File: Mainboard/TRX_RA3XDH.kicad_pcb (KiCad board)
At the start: 2 copper layers, 100 x 100 mm, 203 parts, among them J1 RF_INOUT, J10 MIC_GAIN, J12 PWR, J13 S-Met., J2 VFO, J3 PWR, J4 MIC, J5 VOL, J6 SPK, J8 PTT, J9 CW_KEY, K2 G5V-2, Q1 2N4416, Q10 2N3904, Q12 2N3904, Q2 2N918, Q3 2N4416, Q4 2N918, Q5 2N3904, Q6 2N3904, Q7 2N3904, Q8 2N3904, Q9 2N3906, U1 NE5534, U2 LM386, U3 NE5534, Y1 8.867Mhz, Y2 8.867Mhz, Y3 8.867Mhz, Y4 8.867Mhz, Y5 8.867Mhz, Y6 8.867Mhz, Y7 8.867Mhz, Y8 8.867Mhz

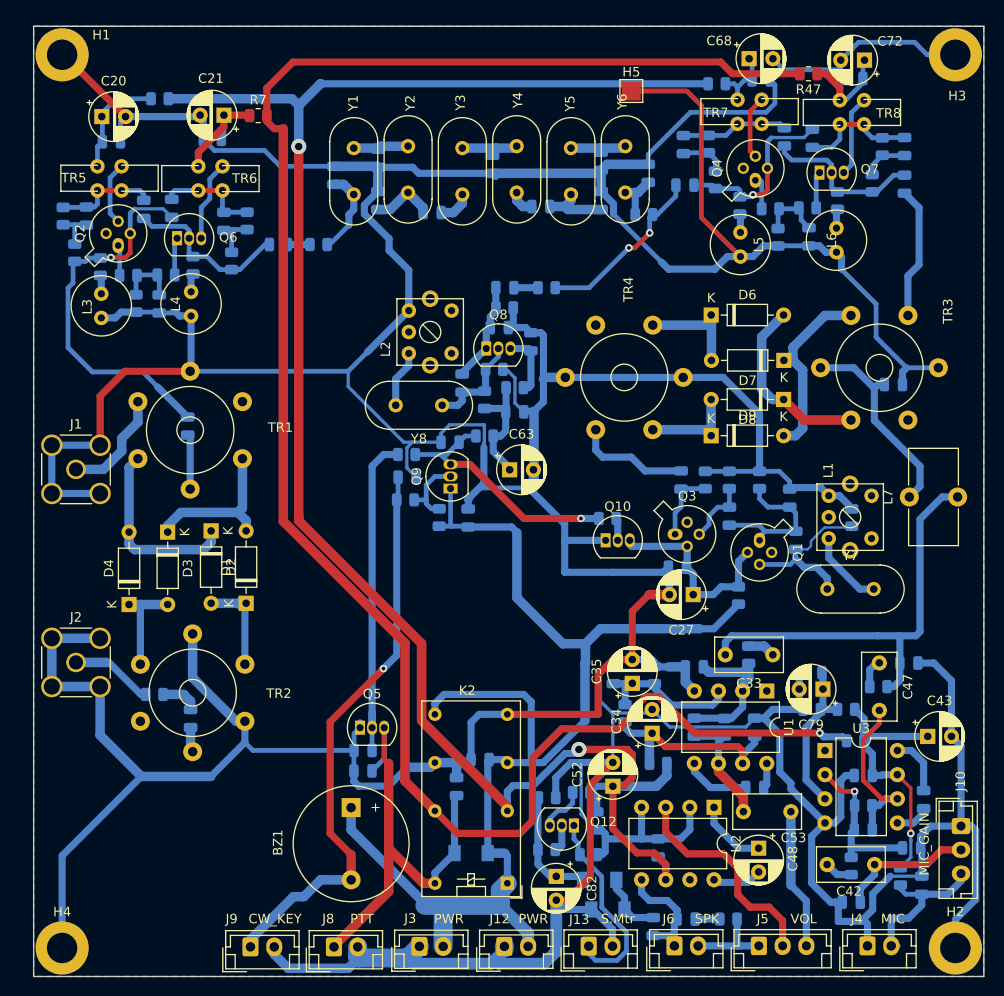
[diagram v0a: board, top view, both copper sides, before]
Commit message: Mainboard is opearational, assembled and tested
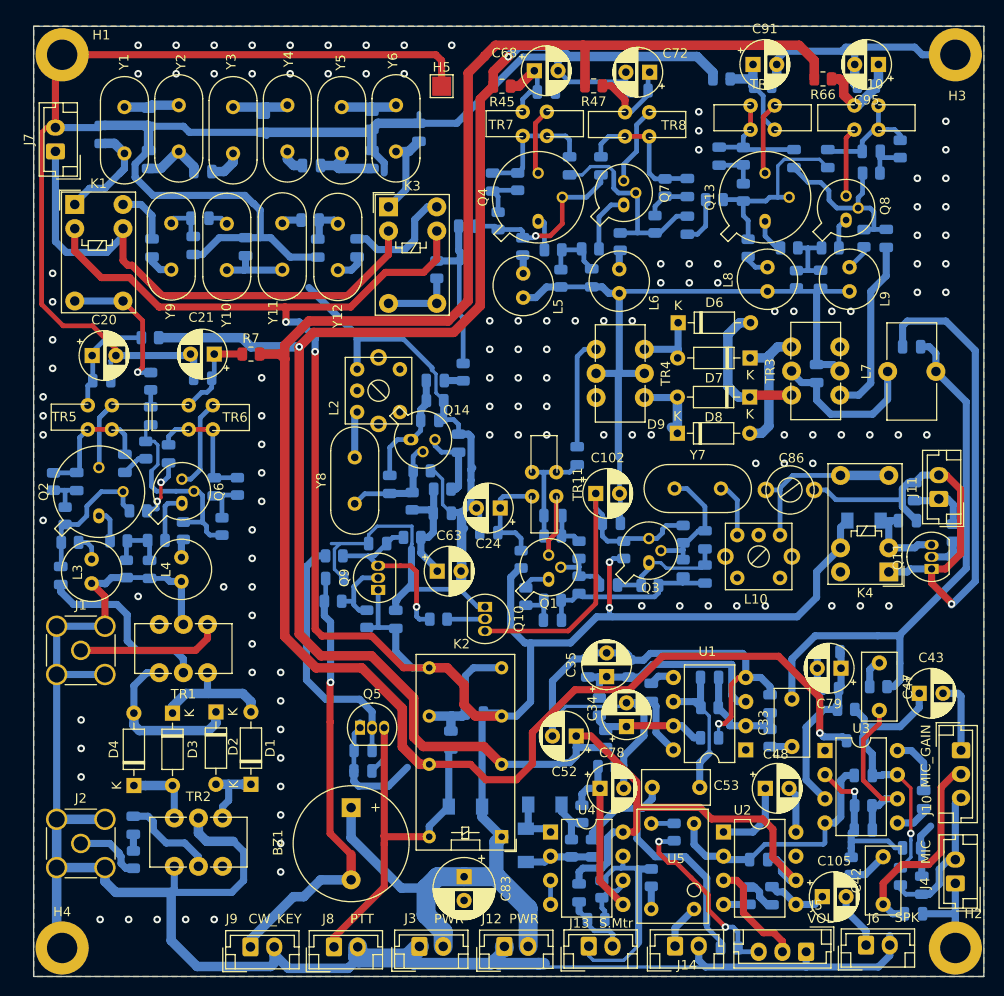
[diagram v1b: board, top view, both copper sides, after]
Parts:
- removed D13, D14: LL4148, Diode_SMD:D_MiniMELF
- removed L1: 3u, NEOSID:NEOSID_5t_4.5x4.5mm_132
- removed Q12: 2N3904, Package_TO_SOT_THT:TO-92_Inline
- added C100: 470p, Capacitor_SMD:C_0805_2012Metric, B.Cu at (109.1, 65.4)
- added C101: 0.1u, Capacitor_SMD:C_0805_2012Metric, B.Cu at (140.8, 97.3)
- added C102: 10u, Capacitor_THT:CP_Radial_D5.0mm_P2.50mm, F.Cu at (139.2, 94.2)
- added C103: 0.1u, Capacitor_SMD:C_0805_2012Metric, B.Cu at (134.6, 107.5)
- added C104: 0.1u, Capacitor_SMD:C_0805_2012Metric, B.Cu at (134.7, 96.5)
- added C105: 10u, Capacitor_THT:CP_Radial_D5.0mm_P2.50mm, F.Cu at (163.0, 136.6)
- added C49: 240p, Capacitor_SMD:C_0805_2012Metric, B.Cu at (92.5, 68.3)
- added C55: 240p, Capacitor_SMD:C_0805_2012Metric, B.Cu at (96.8, 68.1)
- added C81: 390p, Capacitor_SMD:C_0805_2012Metric, B.Cu at (102.3, 68.2)
- added C84: 240p, Capacitor_SMD:C_0805_2012Metric, B.Cu at (109.9, 68.3)
- added C85: 240p, Capacitor_SMD:C_0805_2012Metric, B.Cu at (114.0, 68.3)
- added C86: CTRIM, Ctrimm:Ctrimm_5mm, F.Cu at (159.6, 93.8)
- added C87: 0.1u, Capacitor_SMD:C_0805_2012Metric, B.Cu at (172.0, 97.0)
- added C88: 0.1u, Capacitor_SMD:C_0805_2012Metric, B.Cu at (172.7, 94.0)
- added C89: 0.1u, Capacitor_SMD:C_0805_2012Metric, B.Cu at (156.7, 51.3)
- added C90: 0.1u, Capacitor_SMD:C_0805_2012Metric, B.Cu at (152.1, 58.7)
- added C91: 10u, Capacitor_THT:CP_Radial_D5.0mm_P2.50mm, F.Cu at (155.7, 49.0)
- added C92: 10n, Capacitor_SMD:C_0805_2012Metric, B.Cu at (160.0, 58.9)
- added C93: 10n, Capacitor_SMD:C_0805_2012Metric, B.Cu at (163.6, 58.9)
- added C94: 0.1u, Capacitor_SMD:C_0805_2012Metric, B.Cu at (162.8, 71.6)
- added C95: 10u, Capacitor_THT:CP_Radial_D5.0mm_P2.50mm, F.Cu at (168.9, 49.0)
- added C96: 0.1u, Capacitor_SMD:C_0805_2012Metric, B.Cu at (168.1, 58.2)
- added C97: 0.1u, Capacitor_SMD:C_0805_2012Metric, B.Cu at (167.6, 51.3)
- added C98: 0.1u, Capacitor_SMD:C_0805_2012Metric, B.Cu at (169.7, 67.3)
- added C99: 470p, Capacitor_SMD:C_0805_2012Metric, B.Cu at (97.5, 65.2)
- added D11: LL4148, Diode_SMD:D_MiniMELF, B.Cu at (131.8, 131.2)
- added D12: LL4148, Diode_SMD:D_MiniMELF, B.Cu at (133.8, 126.9)
- added D5: LL4148, Diode_SMD:D_MiniMELF, B.Cu at (167.4, 97.0)
- added J11: USB, Connector_JST:JST_EH_B2B-EH-A_1x02_P2.50mm_Vertical, F.Cu at (175.3, 94.7)
- added J14: AGC, Connector_JST:JST_EH_B2B-EH-A_1x02_P2.50mm_Vertical, F.Cu at (147.5, 141.8)
- added J7: CW_FLT, Connector_JST:JST_EH_B2B-EH-A_1x02_P2.50mm_Vertical, F.Cu at (82.3, 58.2)
- added K1: G5V-1, Relay_THT:Relay_SPDT_Omron_G5V-1, F.Cu at (84.3, 63.8)
- added K3: G5V-1, Relay_THT:Relay_SPDT_Omron_G5V-1, F.Cu at (117.3, 64.0)
- added K4: G5V-1, Relay_THT:Relay_SPDT_Omron_G5V-1, F.Cu at (170.0, 102.4)
- added L10: 3u, NEOSID:NEOSID_5t_4.5x4.5mm_132, F.Cu at (154.1, 98.5)
- added L8: 33u, Inductor:L2.5x6, F.Cu at (157.2, 71.6)
- added L9: 33u, Inductor:L2.5x6, F.Cu at (165.9, 71.6)
- added Q11: 2N3904, Package_TO_SOT_THT:TO-92_Inline, F.Cu at (174.5, 102.1)
- added Q13: 2N5109, Package_TO_SOT_THT:TO-5-3, F.Cu at (157.0, 65.5)
- added Q14: 2N2222, Package_TO_SOT_THT:TO-18-3, F.Cu at (119.7, 88.5)
- added R54: 22k, Resistor_SMD:R_0805_2012Metric, B.Cu at (176.8, 98.3)
- added R55: 47, Resistor_SMD:R_0805_2012Metric, B.Cu at (151.6, 63.2)
- added R56: 470, Resistor_SMD:R_0805_2012Metric, B.Cu at (154.7, 62.5)
- added R61: 470, Resistor_SMD:R_0805_2012Metric, B.Cu at (155.2, 68.3)
- added R62: 2.2k, Resistor_SMD:R_0805_2012Metric, B.Cu at (154.7, 58.7)
- added R63: 4.7, Resistor_SMD:R_0805_2012Metric, B.Cu at (159.5, 68.3)
- added R64: 47, Resistor_SMD:R_0805_2012Metric, B.Cu at (152.4, 50.5)
- added R65: 100, Resistor_SMD:R_0805_2012Metric, B.Cu at (160.3, 71.6)
- added R66: 47, Resistor_SMD:R_0805_2012Metric, F.Cu at (163.1, 50.5)
- added R67: 8.2, Resistor_SMD:R_0805_2012Metric, B.Cu at (163.8, 68.3)
- added R68: 2.2k, Resistor_SMD:R_0805_2012Metric, B.Cu at (171.2, 57.9)
- added R69: 270, Resistor_SMD:R_0805_2012Metric, B.Cu at (168.1, 60.5)
- added R70: 470, Resistor_SMD:R_0805_2012Metric, B.Cu at (167.4, 67.3)
- added R71: 360, Resistor_SMD:R_0805_2012Metric, B.Cu at (144.8, 103.8)
- added R72: 6.8k, Resistor_SMD:R_0805_2012Metric, B.Cu at (148.3, 102.0)
- added R73: 13k, Resistor_SMD:R_0805_2012Metric, B.Cu at (148.3, 98.5)
- added R74: 270, Resistor_SMD:R_0805_2012Metric, B.Cu at (142.1, 100.1)
- added R75: 2.2k, Resistor_SMD:R_0805_2012Metric, B.Cu at (134.6, 98.7)
- added R76: 100, Resistor_SMD:R_0805_2012Metric, B.Cu at (145.0, 134.6)
- added R77: 2k, Resistor_SMD:R_0805_2012Metric, B.Cu at (153.2, 142.0)
- added R78: 10k*, Resistor_SMD:R_0805_2012Metric, B.Cu at (139.2, 139.0)
- added R79: 10k, Resistor_SMD:R_0805_2012Metric, B.Cu at (139.8, 135.8)
- added R80: 33*, Resistor_SMD:R_0805_2012Metric, B.Cu at (91.0, 96.0)
- added R81: 33*, Resistor_SMD:R_0805_2012Metric, B.Cu at (91.8, 89.6)
- added R82: 1k, Resistor_SMD:R_0805_2012Metric, B.Cu at (147.4, 129.8)
- added TR10: FT37-43, Inductor:L_Toroid_Vertical_L10.0mm_W5.0mm_4pin, F.Cu at (167.6, 53.3)
- added TR11: FT37-43, Inductor:L_Toroid_Vertical_L10.0mm_W5.0mm_4pin, F.Cu at (135.0, 93.2)
- added TR9: FT37-43, Inductor:L_Toroid_Vertical_L10.0mm_W5.0mm_4pin, F.Cu at (156.7, 53.3)
- added U4: LM358, Package_DIP:DIP-8_W7.62mm, F.Cu at (134.4, 129.8)
- added U5: LCR0202, Vactrol:lcr0202, F.Cu at (145.0, 137.9)
- added Y10: 8Mhz, Crystal:Crystal_HC49-U_Vertical, F.Cu at (100.3, 65.8)
- added Y11: 8Mhz, Crystal:Crystal_HC49-U_Vertical, F.Cu at (106.2, 70.6)
- added Y12: 8Mhz, Crystal:Crystal_HC49-U_Vertical, F.Cu at (112.0, 65.8)
- added Y9: 8Mhz, Crystal:Crystal_HC49-U_Vertical, F.Cu at (94.5, 70.6)
- C10, C14: value 120p -> 100p
- C11, C13: value 370p -> 330p
- C12: value 130p -> 120p
- C15, C9: value 94p -> 100p
- C16, C8: value 43p -> 39p
- C24: value 22p -> 10u; footprint Capacitor_SMD:C_0805_2012Metric -> Capacitor_THT:CP_Radial_D5.0mm_P2.50mm; moved to F.Cu
- C25: value 22p -> 0.1u
- C27: value 10u -> 22p; footprint Capacitor_THT:CP_Radial_D5.0mm_P2.50mm -> Capacitor_SMD:C_0805_2012Metric; moved to B.Cu
- C28: value 0.1u -> 22p
- C29: value 33p -> 22p
- C78: value 0.1u -> 1u; footprint Capacitor_SMD:C_0805_2012Metric -> Capacitor_THT:CP_Radial_D5.0mm_P2.50mm; moved to F.Cu
- C82: value 4.7u -> 0.1u; footprint Capacitor_THT:CP_Radial_D5.0mm_P2.50mm -> Capacitor_SMD:C_0805_2012Metric; moved to B.Cu
- C83: value 0.1u -> 100u; footprint Capacitor_SMD:C_0805_2012Metric -> Capacitor_THT:CP_Radial_D6.3mm_P2.50mm; moved to F.Cu
- Q1, Q3: value 2N4416 -> 2N2222; footprint Package_TO_SOT_THT:TO-72-4 -> Package_TO_SOT_THT:TO-18-3
- Q2, Q4: value 2N918 -> 2N5109; footprint Package_TO_SOT_THT:TO-72-4 -> Package_TO_SOT_THT:TO-5-3
- Q6, Q7, Q8: value 2N3904 -> 2N2222; footprint Package_TO_SOT_THT:TO-92_Inline -> Package_TO_SOT_THT:TO-18-3
- R19: value 680 -> 270
- R20: value 680 -> 100
- R21: value 10k -> 33*
- R45: moved to F.Cu
- R48: value 4.7 -> 8.2
- R50: value 470 -> 270
- R52: value 1k -> 100
- R53: value 10k -> 680
- R57: value 1M -> 1k
- R58: value 150k -> 33k
- R59: value 8.2k -> 100
- R60: value 1k -> 470k
- TR1, TR2, TR3, TR4: footprint Transformer_THT:Transformer_Toroid_Tapped_Horizontal_D9.0mm_Amidon-T30 -> Inductor:L_Toroid_Vertical_L10.0mm_W5.0mm_6pin
- Y1, Y2, Y3, Y4, Y5, Y6: value 8.867Mhz -> 8Mhz
- moved Q8 40.2 mm to (165.5, 65.4), turned to 90 degrees
- moved C80 33.3 mm to (172.4, 78.7), turned to 180 degrees
- moved C25 31.9 mm to (127.9, 98.3), turned to 180 degrees
- moved C24 31.3 mm to (129.1, 95.7), turned to 180 degrees
- moved R53 29.6 mm to (137.4, 103.8), turned to 270 degrees
- moved R2 29.2 mm to (83.8, 99.3), turned to 180 degrees
- moved Q2 28.5 mm to (86.9, 96.5)
- moved R14 28.0 mm to (99.8, 97.6)
- moved R15 28.0 mm to (95.8, 98.1)
- moved R4 28.0 mm to (89.0, 99.2)
- moved C17 28.0 mm to (92.2, 102.2)
- moved C18 28.0 mm to (99.0, 93.5)
- moved C2 28.0 mm to (84.5, 92.9)
- moved L3 28.0 mm to (86.1, 102.4)
- moved L4 28.0 mm to (95.6, 102.2)
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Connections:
- C24 pad 2: Net-(C24-Pad2) -> GND
- C25 pad 1: Net-(C24-Pad2) -> Net-(C24-Pad1)
- C26 pad 1: Net-(C26-Pad1) -> Net-(C104-Pad1)
- C27 pad 2: GND -> Net-(C27-Pad2)
- C28 pad 1: Net-(C27-Pad1) -> Net-(C28-Pad1)
- C28 pad 2: GND -> Net-(C27-Pad1)
- C29 pad 1: Net-(C29-Pad1) -> Net-(C27-Pad1)
- C29 pad 2: Net-(C24-Pad2) -> GND
- C54 pad 2: Net-(C54-Pad2) -> Net-(C105-Pad1)
- C6 pad 2: Net-(C1-Pad1) -> Net-(C6-Pad2)
- C7 pad 2: Net-(C3-Pad1) -> Net-(C7-Pad2)
- C75 pad 1: Net-(C69-Pad1) -> Net-(C75-Pad1)
- C75 pad 2: Net-(C75-Pad2) -> Net-(C69-Pad1)
- C78 pad 2: Net-(C54-Pad2) -> GND
- C82 pad 1: Net-(C82-Pad1) -> /+12V_RX
- C83 pad 1: /+12V_RX -> +12V
- J5 pad 3: /VOL_IN -> Net-(J5-Pad3)
- J6 pad 1: Net-(C54-Pad2) -> Net-(C105-Pad2)
- Q1 pad 1: Net-(C24-Pad2) -> Net-(Q1-Pad1)
- Q1 pad 2: Net-(C27-Pad1) -> Net-(C27-Pad2)
- Q1 pad 3: Net-(C24-Pad1) -> Net-(Q1-Pad3)
- Q10 pad 3: Net-(C27-Pad1) -> Net-(C101-Pad1)
- Q3 pad 1: Net-(C26-Pad1) -> Net-(C27-Pad1)
- Q3 pad 2: Net-(C27-Pad1) -> Net-(C28-Pad1)
- Q3 pad 3: Net-(C29-Pad1) -> Net-(C101-Pad1)
- Q6 pad 2: Net-(C3-Pad1) -> Net-(C7-Pad2)
- Q8 pad 1: Net-(C58-Pad1) -> Net-(Q8-Pad1)
- Q8 pad 2: Net-(C59-Pad1) -> Net-(C92-Pad1)
- Q8 pad 3: Net-(C57-Pad1) -> Net-(Q8-Pad3)
- R10 pad 1: Net-(C8-Pad1) -> Net-(K1-Pad5)
- R11 pad 2: Net-(C16-Pad1) -> Net-(K3-Pad5)
- R14 pad 1: Net-(C3-Pad1) -> Net-(C7-Pad2)
- R15 pad 2: Net-(C3-Pad1) -> Net-(C7-Pad2)
- R19 pad 1: Net-(C24-Pad2) -> +12V
- R19 pad 2: GND -> Net-(C24-Pad1)
- R20 pad 1: Net-(C27-Pad1) -> Net-(C103-Pad1)
- R20 pad 2: +12V -> GND
- R21 pad 1: Net-(C29-Pad1) -> Net-(Q1-Pad1)
- R21 pad 2: GND -> Net-(C103-Pad1)
- R22 pad 1: Net-(C26-Pad1) -> Net-(C104-Pad2)
- R22 pad 2: GND -> Net-(C27-Pad2)
- R53 pad 1: Net-(C24-Pad1) -> Net-(C27-Pad2)
- R57 pad 1: Net-(C82-Pad1) -> /VOL_IN
- R57 pad 2: GND -> Net-(D11-Pad2)
- R58 pad 1: Net-(Q12-Pad2) -> Net-(D11-Pad2)
- R58 pad 2: Net-(C82-Pad1) -> Net-(D12-Pad1)
- R59 pad 1: Net-(Q12-Pad3) -> Net-(D12-Pad1)
- R59 pad 2: /+12V_RX -> Net-(C78-Pad1)
- R60 pad 1: GND -> Net-(C78-Pad1)
- R60 pad 2: Net-(J13-Pad1) -> GND
- TR3 pad 4: Net-(C75-Pad2) -> Net-(C98-Pad1)
- U2 pad 5: Net-(C54-Pad2) -> Net-(C105-Pad1)
- Y7 pad 1: Net-(C24-Pad1) -> Net-(C28-Pad1)
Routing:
- net +12V: track 134.4 -> 249.5 mm, vias 0 -> 4
- net Net-(J7-Pad1): track 0.00 -> 55.7 mm
- net Net-(C101-Pad1): track 0.00 -> 38.8 mm
- net GND: track 837.7 -> 874.9 mm, vias 0 -> 119
- net Net-(C1-Pad1): track 40.3 -> 15.1 mm, vias 1 -> 0
- net Net-(C7-Pad2): track 0.00 -> 22.0 mm
- net Net-(C93-Pad2): track 0.00 -> 20.6 mm
- net Net-(J5-Pad3): track 0.00 -> 19.6 mm, vias 0 -> 2
- net Net-(C92-Pad1): track 0.00 -> 19.0 mm
- net Net-(C98-Pad1): track 0.00 -> 18.7 mm
- net Net-(C86-Pad1): track 0.00 -> 18.5 mm
- net /+12V_RX: track 192.5 -> 210.1 mm
- net Net-(C24-Pad2): track 15.8 -> 0.00 mm
- net Net-(K1-Pad5): track 0.00 -> 15.3 mm, vias 0 -> 1
- net /VOL_IN: track 14.8 -> 29.9 mm
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
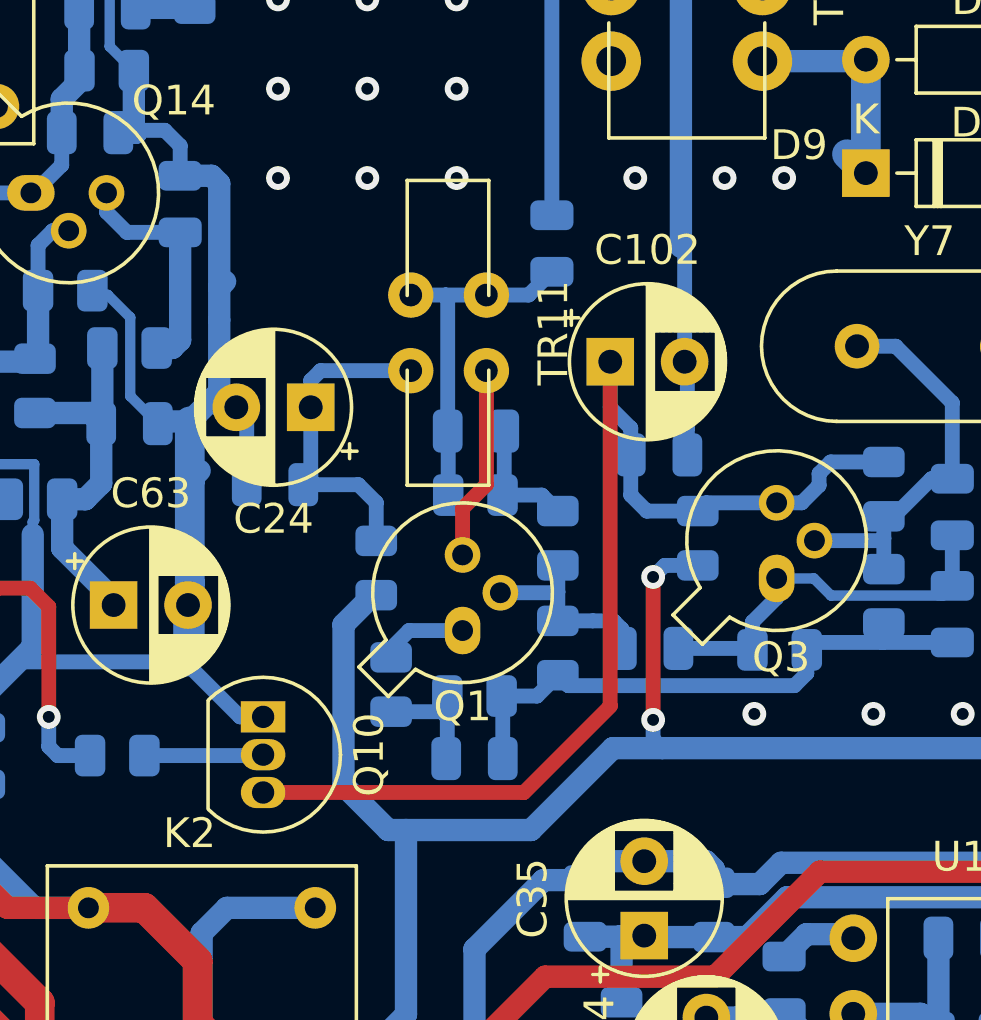
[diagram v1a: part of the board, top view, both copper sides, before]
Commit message: Add 6-Band band N7DDC pass filter
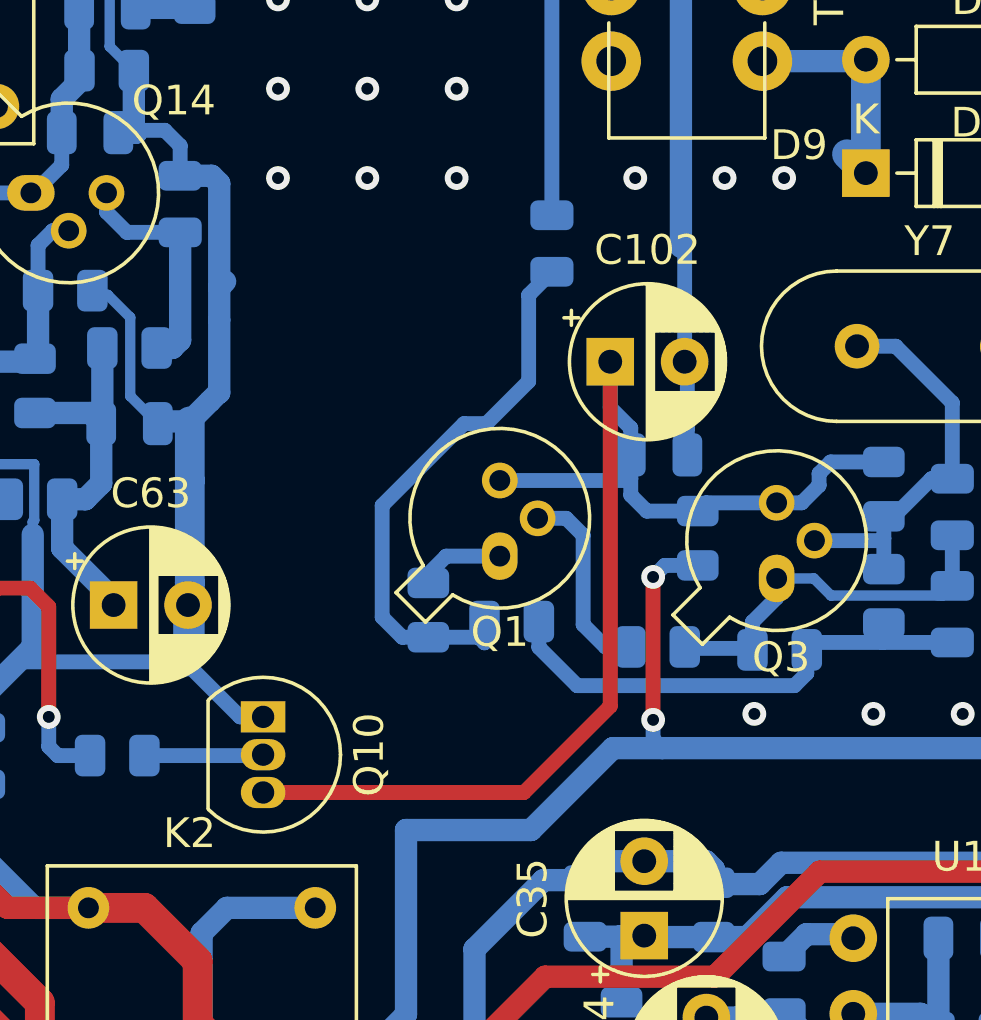
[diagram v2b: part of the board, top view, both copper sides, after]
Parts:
- removed C103, C104, C25: 0.1u, Capacitor_SMD:C_0805_2012Metric
- removed C24: 10u, Capacitor_THT:CP_Radial_D5.0mm_P2.50mm
- removed C27: 22p, Capacitor_SMD:C_0805_2012Metric
- removed R19: 270, Resistor_SMD:R_0805_2012Metric
- removed R53: 680, Resistor_SMD:R_0805_2012Metric
- removed R75: 2.2k, Resistor_SMD:R_0805_2012Metric
- removed TR11: FT37-43, Inductor:L_Toroid_Vertical_L10.0mm_W5.0mm_4pin
- R22: value 470 -> 1.5k
- R74: value 270 -> 100
- moved R22 4.95 mm to (140.8, 103.8), turned to 180 degrees
- moved Q1 2.80 mm to (135.4, 100.7)
- moved R20 2.80 mm to (135.8, 102.9)
- moved R21 2.80 mm to (133.1, 102.5)
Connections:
- C26 pad 1: Net-(C104-Pad1) -> Net-(C26-Pad1)
- C28 pad 2: Net-(C27-Pad1) -> Net-(C28-Pad2)
- C29 pad 1: Net-(C27-Pad1) -> Net-(C28-Pad2)
- Q1 pad 3: Net-(Q1-Pad3) -> Net-(C101-Pad1)
- Q3 pad 1: Net-(C27-Pad1) -> Net-(C28-Pad2)
- R20 pad 1: Net-(C103-Pad1) -> Net-(C26-Pad1)
- R21 pad 2: Net-(C103-Pad1) -> Net-(C26-Pad1)
- R22 pad 1: Net-(C104-Pad2) -> Net-(C28-Pad2)
- R71 pad 1: Net-(C27-Pad1) -> Net-(C28-Pad2)
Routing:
- net Net-(C26-Pad1): track 0.00 -> 18.9 mm
- net Net-(C28-Pad2): track 0.00 -> 13.3 mm
- net Net-(C27-Pad1): track 13.3 -> 0.00 mm
- net Net-(C104-Pad1): track 11.8 -> 0.00 mm
- net Net-(C24-Pad1): track 11.1 -> 0.00 mm
- net +12V: track 249.5 -> 239.9 mm
- net GND: track 874.9 -> 868.3 mm
- net Net-(Q1-Pad3): track 6.52 -> 0.00 mm
- net Net-(C101-Pad1): track 38.8 -> 43.3 mm
- net Net-(C104-Pad2): track 4.25 -> 0.00 mm
- net Net-(C103-Pad1): track 4.08 -> 0.00 mm
